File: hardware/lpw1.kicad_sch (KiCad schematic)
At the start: 14 parts, among them J7 JST PH2P ST, Q2 PMOS AS3401, U9 MCP73831-2

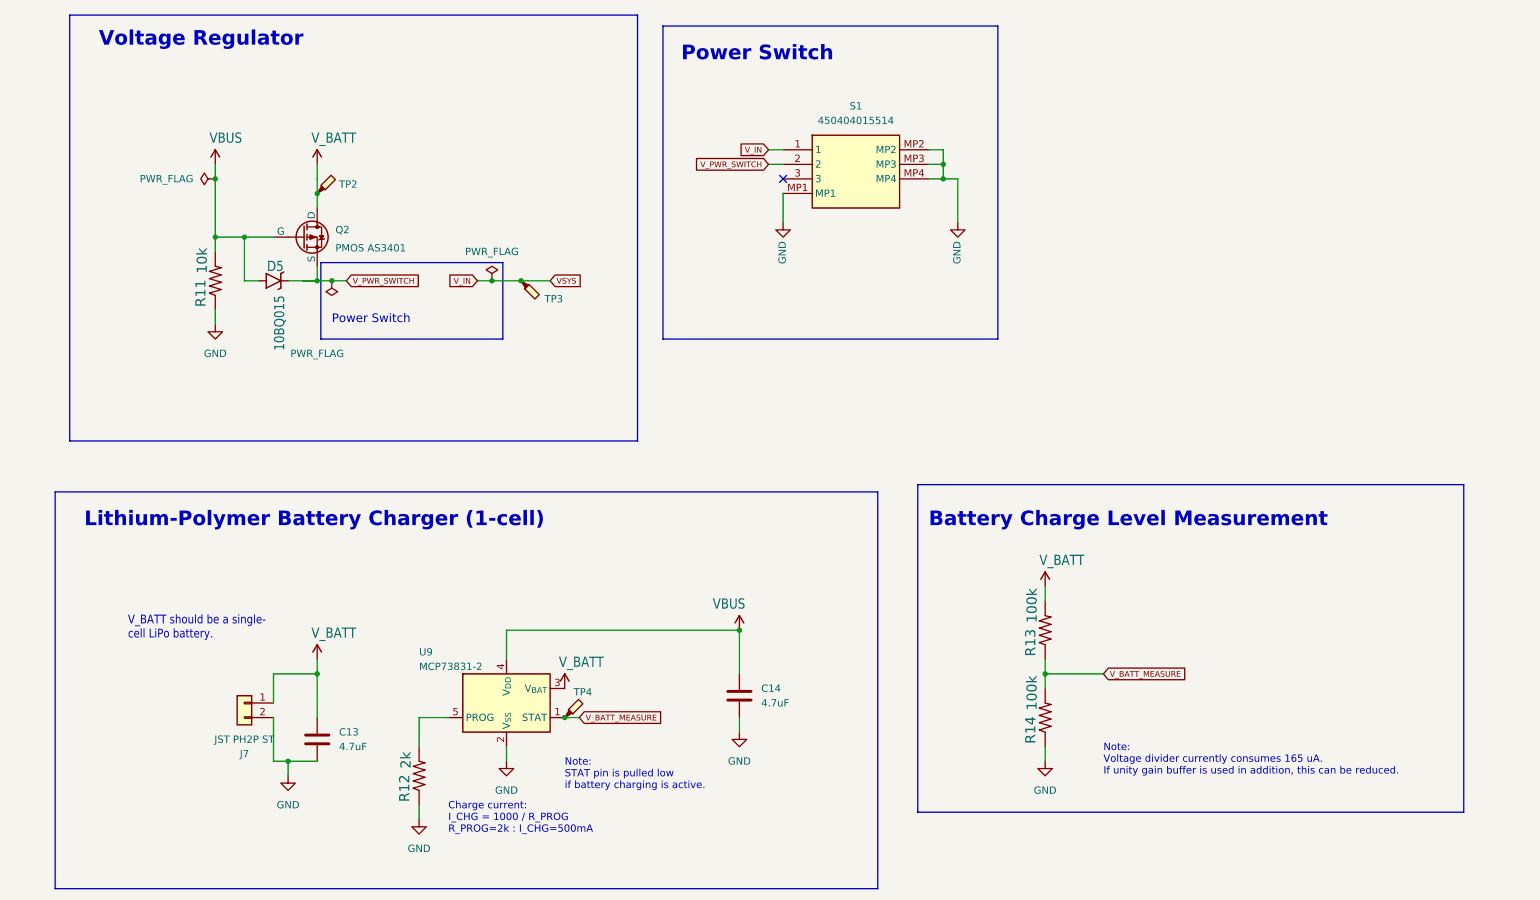
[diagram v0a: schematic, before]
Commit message: Added solder jumper between BAT and p-MOS; Rewired battery level measurem. to GPIO pin in order to have it off when not needed; Changed all Rs into EU Rs; Renamed all components for them to be uniform; Removed Schottky since Pico W has its own built in as well as pulldown R; Changed p-MOSFET to recommended p-MOS in 28 page datasheet (Pico W); Changed Footprint of Audio AMP, rewired too;
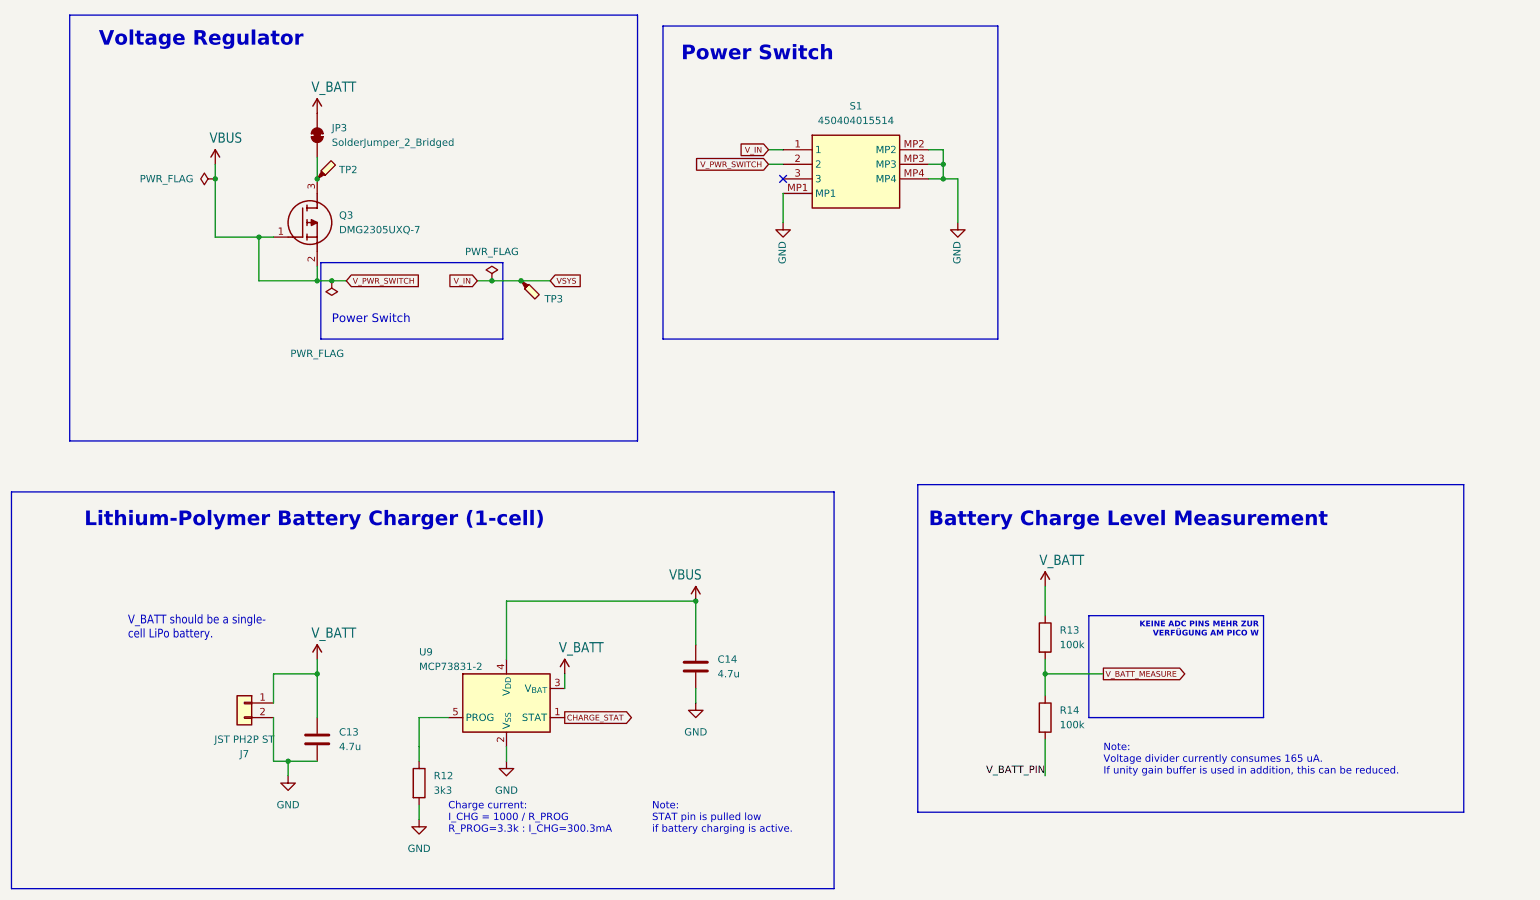
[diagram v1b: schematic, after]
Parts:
- removed D5: 10BQ015, Diode_SMD:D_SMB_Handsoldering, symbol esp32-thing-eagle-import:DIODE-SCHOTTKY-BAT20J
- removed Q2: PMOS AS3401, Package_TO_SOT_SMD:TSOT-23_HandSoldering, symbol HeadMouse:AS3401
- removed R11: 10k, Resistor_SMD:R_0603_1608Metric_Pad0.98x0.95mm_HandSolder, symbol esp32-thing-eagle-import:27OHM1/10W1%(0603)0603-RES
- removed R12: 2k, Resistor_SMD:R_0603_1608Metric_Pad0.98x0.95mm_HandSolder, symbol esp32-thing-eagle-import:27OHM1/10W1%(0603)0603-RES
- removed R13, R14: 100k, Resistor_SMD:R_0603_1608Metric_Pad0.98x0.95mm_HandSolder, symbol esp32-thing-eagle-import:27OHM1/10W1%(0603)0603-RES
- removed TP4: TestPoint_Probe, TestPoint:TestPoint_THTPad_D2.0mm_Drill1.0mm, symbol Connector:TestPoint_Probe
- added JP3: SolderJumper_2_Bridged, Jumper:SolderJumper-2_P1.3mm_Bridged_RoundedPad1.0x1.5mm, symbol Jumper:SolderJumper_2_Bridged
- added Q3: DMG2305UXQ-7, p-MOS:SOT96P240X110-3N, symbol DMG2305UXQ-7:DMG2305UXQ-7
- added R12: 3k3, Resistor_SMD:R_0603_1608Metric, symbol Device:R
- added R13, R14: 100k, R_0603_1608Metric, symbol Device:R
- C13, C14: value 4.7uF -> 4.7u; footprint Capacitor_SMD:C_0603_1608Metric_Pad1.08x0.95mm_HandSolder -> Capacitor_SMD:C_0603_1608Metric
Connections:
- net V_PWR_SWITCH is gone; now on net VBUS: S1.2
- net GND: now also R12.2
- net VBUS: now also Q3.1 (G), Q3.2 (S)
- net V_BATT: now also JP3.2 (B), R13.1; no longer TP2.1
- net V_BATT_MEASURE: now also R13.2, R14.1; no longer U9.1 (STAT)
- net at U9.5 (PROG): now also R12.1
- new net: JP3.1 (A), Q3.3 (D), TP2.1
- new net CHARGE_STAT: U9.1 (STAT)
- new net V_BATT_PIN: R14.2
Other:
- note added: "Charge current: I_CHG = 1000 / R_PROG R_PROG=3.3k : I_CHG=300.3mA"
- note removed: "Charge current: I_CHG = 1000 / R_PROG R_PROG=2k : I_CHG=500mA"
- moved on the sheet: C14, TP2

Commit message: Done more finetuning; No more ADC Pin on the Pico W left, waiting for response/recommendation of prof.; Made sure that every route is correct; Added new GPIO inputs, namely voltage divider so it would not constantly draw current (V_BATT_VD_SWITCH), (CHARGE_STAT) from the MCP STAT pin;
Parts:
- removed Q3: DMG2305UXQ-7, p-MOS:SOT96P240X110-3N, symbol DMG2305UXQ-7:DMG2305UXQ-7
- added Q2: DMG2305UXQ-7, p-MOS:SOT96P240X110-3N, symbol DMG2305UXQ-7:DMG2305UXQ-7
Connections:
- net VBUS: now also Q2.1 (G), Q2.2 (S)
- net at JP3.1 (A), TP2.1: now also Q2.3 (D)
- net V_BATT_PIN renamed V_BATT_VD_SWITCH
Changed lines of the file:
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@@
+	)
+	(junction
+		(at 68.58 48.26)
+		(diameter 0)
+		(color 0 0 0 0)
 	)
 	(junction
@@
 	(junction
 		(at 99.06 66.04)
-		(diameter 0)
-		(color 0 0 0 0)
-	)
-	(junction
-		(at 68.58 48.26)
 		(diameter 0)
 		(color 0 0 0 0)
@@
 			)
 			(justify left bottom)
-		)
-	)
-	(label "V_BATT_PIN"
-		(at 195.58 152.4 180)
-		(fields_autoplaced yes)
-		(effects
-			(font
-				(size 1.27 1.27)
-			)
-			(justify right bottom)
 		)
 	)
@@
 	)
 	(global_label "CHARGE_STAT"
-		(shape output)
+		(shape bidirectional)
 		(at 111.76 142.24 0)
 		(fields_autoplaced yes)
@@
 		)
 		(property "Intersheetrefs" "${INTERSHEET_REFS}"
-			(at 123.3896 142.24 0)
+			(at 124.1326 142.24 0)
 			(effects
 				(font
@@
 	)
 	(global_label "V_IN"
-		(shape input)
+		(shape output)
 		(at 147.32 43.18 180)
 		(fields_autoplaced yes)
@@
 	)
 	(global_label "V_PWR_SWITCH"
-		(shape input)
+		(shape output)
 		(at 73.66 66.04 0)
 		(fields_autoplaced yes)
@@
 				)
 				(justify left)
+				(hide yes)
+			)
+		)
+	)
+	(global_label "V_BATT_VD_SWITCH"
+		(shape bidirectional)
+		(at 195.58 152.4 180)
+		(fields_autoplaced yes)
+		(effects
+			(font
+				(size 0.9906 0.9906)
+			)
+			(justify right)
+		)
+		(property "Intersheetrefs" "${INTERSHEET_REFS}"
+			(at 179.3867 152.4 0)
+			(effects
+				(font
+					(size 1.27 1.27)
+				)
+				(justify right)
 				(hide yes)
 			)
@@
 	)
 	(symbol
+		(lib_id "DMG2305UXQ-7:DMG2305UXQ-7")
+		(at 60.96 58.42 0)
+		(unit 1)
+		(exclude_from_sim no)
+		(in_bom yes)
+		(on_board yes)
+		(dnp no)
+		(fields_autoplaced yes)
+		(property "Reference" "Q2"
+			(at 72.39 54.6099 0)
+			(effects
+				(font
+					(size 1.27 1.27)
+				)
+				(justify left)
+			)
+		)
+		(property "Value" "DMG2305UXQ-7"
+			(at 72.39 57.1499 0)
+			(effects
+				(font
+					(size 1.27 1.27)
+				)
+				(justify left)
+			)
+		)
+		(property "Footprint" "p-MOS:SOT96P240X110-3N"
+			(at 72.39 157.15 0)
+			(effects
+				(font
+					(size 1.27 1.27)
+				)
+				(justify left top)
+				(hide yes)
+			)
+		)
+		(property "Datasheet" "https://www.diodes.com//assets/Datasheets/DMG2305UXQ.pdf"
+			(at 72.39 257.15 0)
+			(effects
+				(font
+					(size 1.27 1.27)
+				)
+				(justify left top)
+				(hide yes)
+			)
+		)
+		(property "Description" "MOSFET MOSFET BVDSS"
+			(at 60.96 58.42 0)
+			(effects
+				(font
+					(size 1.27 1.27)
+				)
+				(hide yes)
+			)
+		)
+		(property "Height" "1.1"
+			(at 72.39 457.15 0)
+			(effects
+				(font
+					(size 1.27 1.27)
+				)
+				(justify left top)
+				(hide yes)
+			)
+		)
+		(property "Mouser Part Number" "621-DMG2305UXQ-7"
+			(at 72.39 557.15 0)
+			(effects
+				(font
+					(size 1.27 1.27)
+				)
+				(justify left top)
+				(hide yes)
+			)
+		)
+		(property "Mouser Price/Stock" "https://www.mouser.co.uk/ProductDetail/Diodes-Incorporated/DMG2305UXQ-7?qs=60RJRzIpcl%2FUiAojHt1c9w%3D%3D"
+			(at 72.39 657.15 0)
+			(effects
+				(font
+					(size 1.27 1.27)
+				)
+				(justify left top)
+				(hide yes)
+			)
+		)
+		(property "Manufacturer_Name" "Diodes Incorporated"
+			(at 72.39 757.15 0)
+			(effects
+				(font
+					(size 1.27 1.27)
+				)
+				(justify left top)
+				(hide yes)
+			)
+		)
+		(property "Manufacturer_Part_Number" "DMG2305UXQ-7"
+			(at 72.39 857.15 0)
+			(effects
+				(font
+					(size 1.27 1.27)
+				)
+				(justify left top)
+				(hide yes)
+			)
+		)
+		(pin "1"
+		)
+		(pin "3"
+		)
+		(pin "2"
+		)
+		(instances
+			(project "FABI_schematic"
+				(path "/8404dabe-a0ce-44ce-a3c9-f9e9e54d2b02/793a4126-d8fb-49c3-b4dd-9f7725c17758"
+					(reference "Q2")
+					(unit 1)
+				)
+			)
+		)
+	)
+	(symbol
 		(lib_id "Battery_Management:MCP73831-2-OT")
 		(at 101.6 139.7 0)
@@
 					(unit 1)
 				)
-			)
-		)
-	)
-	(symbol
-		(lib_id "DMG2305UXQ-7:DMG2305UXQ-7")
-		(at 60.96 58.42 0)
-		(unit 1)
-		(exclude_from_sim no)
-		(in_bom yes)
-		(on_board yes)
-		(dnp no)
-		(fields_autoplaced yes)
-		(property "Reference" "Q3"
-			(at 72.39 54.6099 0)
-			(effects
-				(font
-					(size 1.27 1.27)
-				)
-				(justify left)
-			)
-		)
-		(property "Value" "DMG2305UXQ-7"
-			(at 72.39 57.1499 0)
-			(effects
-				(font
-					(size 1.27 1.27)
-				)
-				(justify left)
-			)
-		)
-		(property "Footprint" "p-MOS:SOT96P240X110-3N"
-			(at 72.39 157.15 0)
-			(effects
-				(font
-					(size 1.27 1.27)
-				)
-				(justify left top)
-				(hide yes)
-			)
-		)
-		(property "Datasheet" "https://www.diodes.com//assets/Datasheets/DMG2305UXQ.pdf"
-			(at 72.39 257.15 0)
-			(effects
-				(font
-					(size 1.27 1.27)
-				)
-				(justify left top)
-				(hide yes)
-			)
-		)
-		(property "Description" "MOSFET MOSFET BVDSS"
-			(at 60.96 58.42 0)
-			(effects
-				(font
-					(size 1.27 1.27)
-				)
-				(hide yes)
-			)
-		)
-		(property "Height" "1.1"
-			(at 72.39 457.15 0)
-			(effects
-				(font
-					(size 1.27 1.27)
-				)
-				(justify left top)
-				(hide yes)
-			)
-		)
-		(property "Mouser Part Number" "621-DMG2305UXQ-7"
-			(at 72.39 557.15 0)
-			(effects
-				(font
-					(size 1.27 1.27)
-				)
-				(justify left top)
-				(hide yes)
-			)
-		)
-		(property "Mouser Price/Stock" "https://www.mouser.co.uk/ProductDetail/Diodes-Incorporated/DMG2305UXQ-7?qs=60RJRzIpcl%2FUiAojHt1c9w%3D%3D"
-			(at 72.39 657.15 0)
-			(effects
-				(font
-					(size 1.27 1.27)
-				)
-				(justify left top)
-				(hide yes)
-			)
-		)
-		(property "Manufacturer_Name" "Diodes Incorporated"
-			(at 72.39 757.15 0)
-			(effects
-				(font
-					(size 1.27 1.27)
-				)
-				(justify left top)
-				(hide yes)
-			)
-		)
-		(property "Manufacturer_Part_Number" "DMG2305UXQ-7"
-			(at 72.39 857.15 0)
-			(effects
-				(font
-					(size 1.27 1.27)
-				)
-				(justify left top)
-				(hide yes)
-			)
-		)
-		(pin "1"
-		)
-		(pin "3"
-		)
-		(pin "2"
-		)
-		(instances
-			(project ""
-				(path "/8404dabe-a0ce-44ce-a3c9-f9e9e54d2b02/793a4126-d8fb-49c3-b4dd-9f7725c17758"
-					(reference "Q3")
-					(unit 1)
-				)

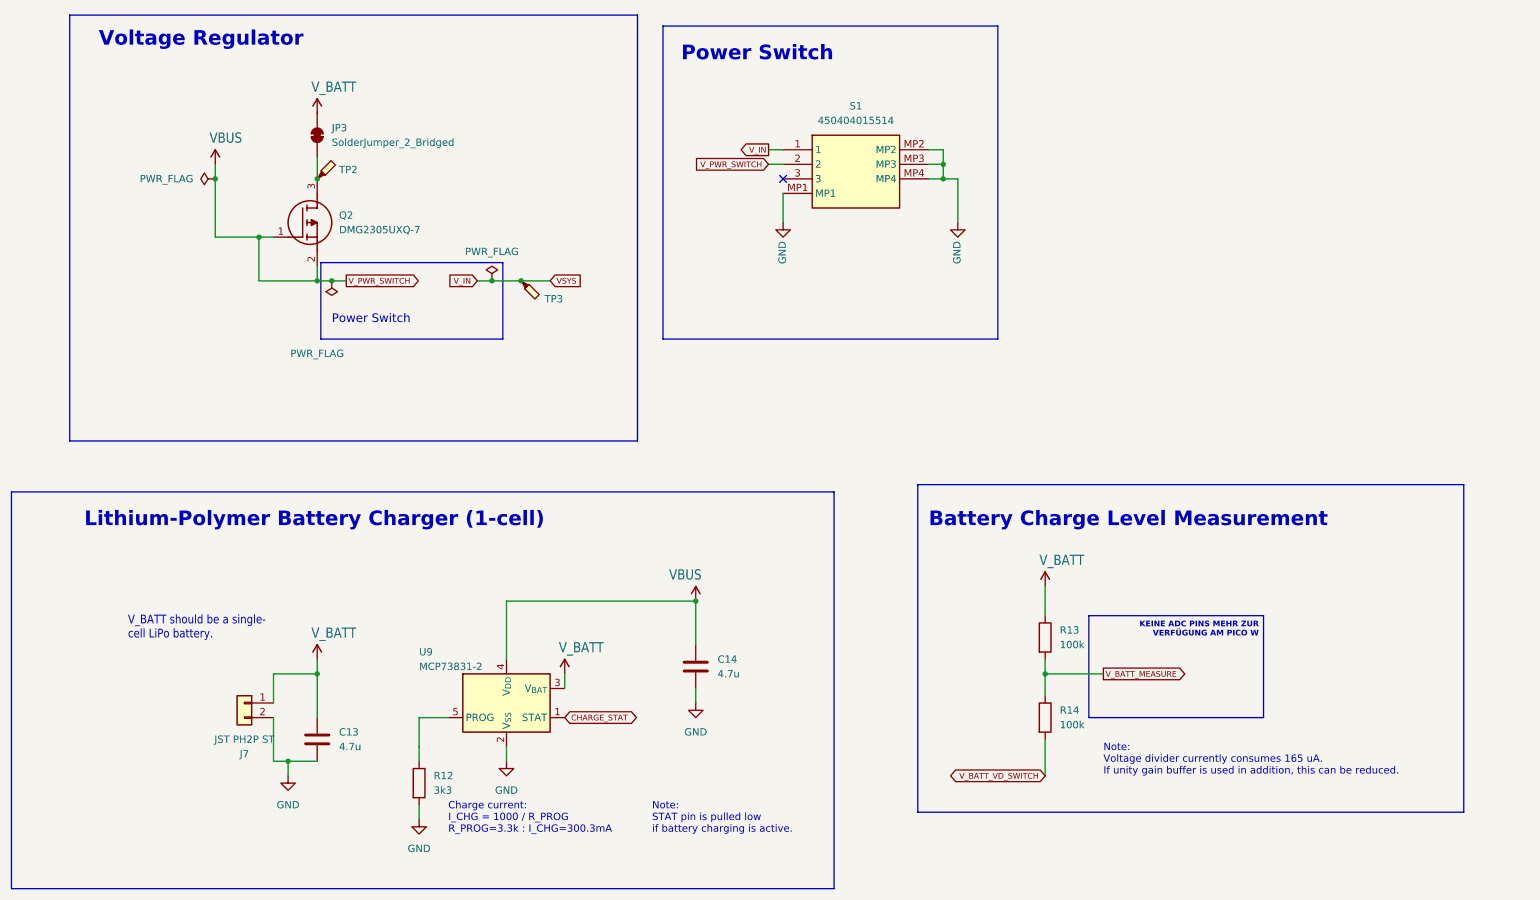
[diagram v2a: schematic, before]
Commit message: Checked for correct wiring of new conductor tracks (new, in the scope of this project); Layout improved;
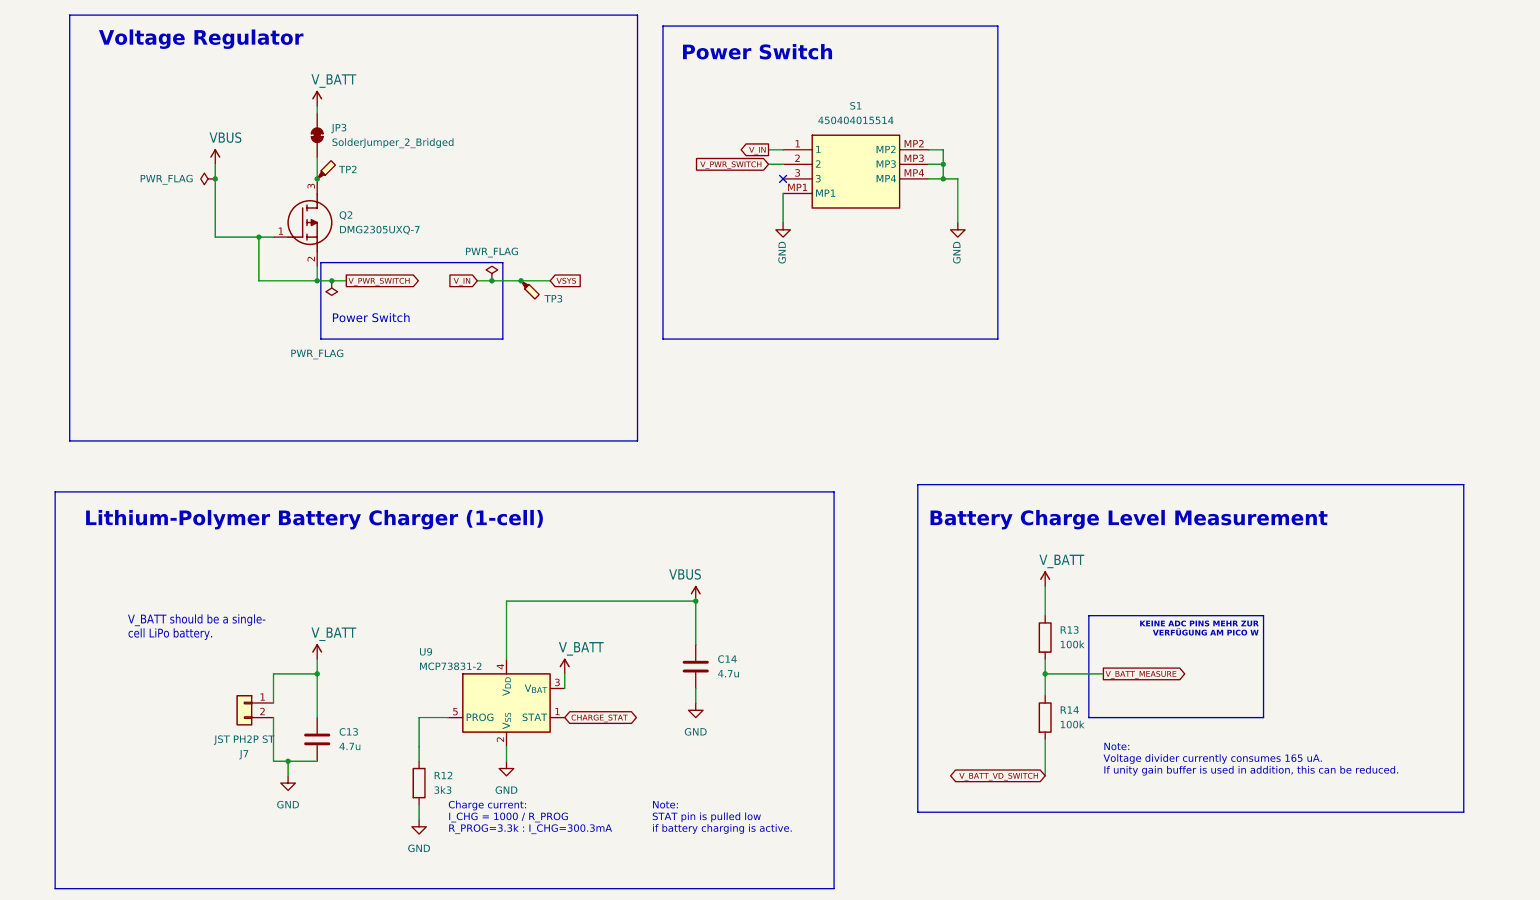
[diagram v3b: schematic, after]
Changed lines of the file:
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@@
+	(wire
+		(pts
+			(xy 68.58 35.56) (xy 68.58 36.83)
+		)
+		(stroke
+			(width 0)
+			(type default)
+		)
+	)
 	(wire
 		(pts
@@
 	)
 	(rectangle
-		(start 15.24 102.87)
+		(start 22.86 102.87)
 		(end 158.75 172.085)
 		(stroke
@@
 	(symbol
 		(lib_id "esp32-thing-eagle-import:V_BATT")
-		(at 68.58 36.83 0)
+		(at 68.58 35.56 0)
 		(unit 1)
 		(exclude_from_sim no)
@@
 		(dnp no)
 		(property "Reference" "#SUPPLY02"
-			(at 68.58 36.83 0)
+			(at 68.58 35.56 0)
 			(effects
 				(font
@@
 		)
 		(property "Value" "V_BATT"
-			(at 67.564 33.274 0)
+			(at 67.564 32.004 0)
 			(effects
 				(font
@@
 		)
 		(property "Footprint" ""
-			(at 68.58 36.83 0)
+			(at 68.58 35.56 0)
 			(effects
 				(font
@@
 		)
 		(property "Datasheet" ""
-			(at 68.58 36.83 0)
+			(at 68.58 35.56 0)
 			(effects
 				(font
@@
 		)
 		(property "Description" ""
-			(at 68.58 36.83 0)
-			(effects
-				(font
+			(at 68.58 35.56 0)
+			(effects
+				(font
